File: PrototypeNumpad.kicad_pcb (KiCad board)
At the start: 2 copper layers, 99 x 99 mm, 92 parts, among them J0 Conn_01x06, J1 USB_B_Micro, J1A1 Conn_01x04, Q1 2N7002, SW0 SW_Push, U1 ATmega32U4-AU, U2 USBLC6-2SC6, Y1 Crystal_GND24

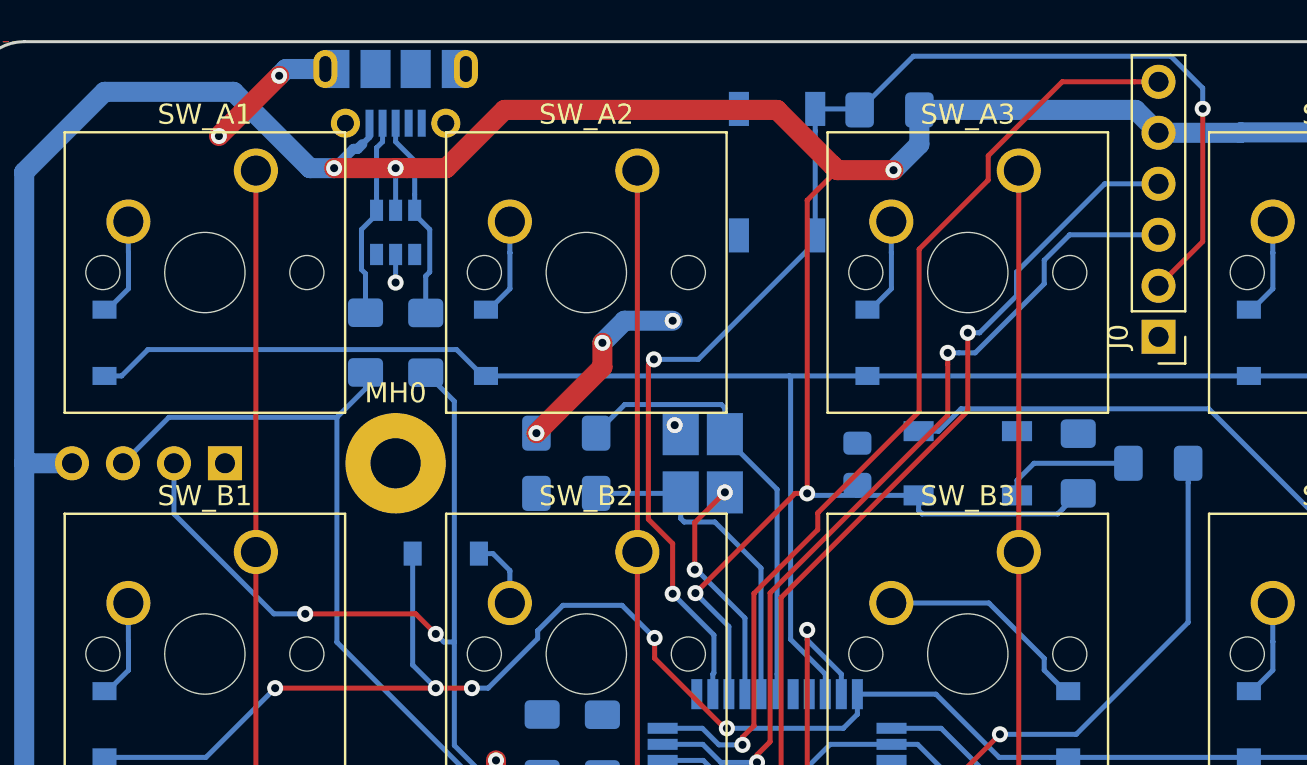
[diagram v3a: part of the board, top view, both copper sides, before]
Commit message: Organize pin headers
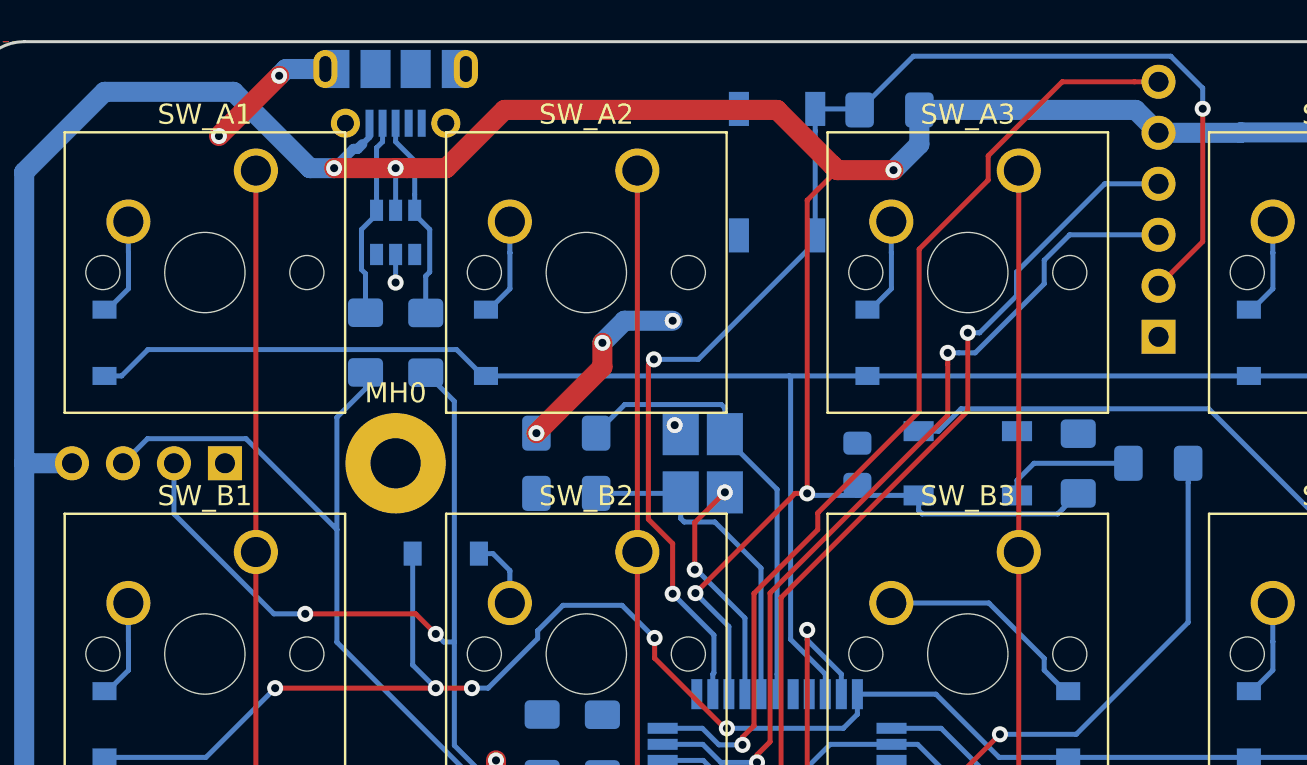
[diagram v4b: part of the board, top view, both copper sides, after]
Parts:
- J0: moved to B.Cu
- turned J0 to 0 degrees
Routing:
- net D-: track 46.3 -> 47.7 mm
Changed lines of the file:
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@@
     (thickness 1.6)
     (drawings 18)
-    (tracks 670)
+    (tracks 672)
     (zones 0)
     (modules 92)
@@
     )
   )
-  (module Connector_PinHeader_2.54mm:PinHeader_1x06_P2.54mm_Vertical (layer F.Cu)
-    (at 107.5 43.2 180)
+  (module Connector_PinHeader_2.54mm:PinHeader_1x06_P2.54mm_Vertical (layer B.Cu)
+    (at 107.5 43.2)
     (descr "Through hole straight pin header, 1x06, 2.54mm pitch, single row")
     (tags "Through hole pin header THT 1x06 2.54mm single row")
-    (fp_text reference J0 (at 2 0 90) (layer F.SilkS)
-      (effects (font (size 1 1) (thickness 0.15)))
+    (fp_text reference J0 (at -2 0 90) (layer B.Fab)
+      (effects (font (size 1 1) (thickness 0.15)) (justify mirror))
     )
-    (fp_text value Conn_01x06 (at 0 15.03 180) (layer F.Fab)
-      (effects (font (size 1 1) (thickness 0.15)))
+    (fp_text value Conn_01x06 (at 0 -15.03) (layer B.Fab)
+      (effects (font (size 1 1) (thickness 0.15)) (justify mirror))
     )
-    (fp_line (start -0.635 -1.27) (end 1.27 -1.27) (layer F.Fab) (width 0.1))
-    (fp_line (start 1.27 -1.27) (end 1.27 13.97) (layer F.Fab) (width 0.1))
-    (fp_line (start 1.27 13.97) (end -1.27 13.97) (layer F.Fab) (width 0.1))
-    (fp_line (start -1.27 13.97) (end -1.27 -0.635) (layer F.Fab) (width 0.1))
-    (fp_line (start -1.27 -0.635) (end -0.635 -1.27) (layer F.Fab) (width 0.1))
-    (fp_line (start -1.33 14.03) (end 1.33 14.03) (layer F.SilkS) (width 0.12))
-    (fp_line (start -1.33 1.27) (end -1.33 14.03) (layer F.SilkS) (width 0.12))
-    (fp_line (start 1.33 1.27) (end 1.33 14.03) (layer F.SilkS) (width 0.12))
-    (fp_line (start -1.33 1.27) (end 1.33 1.27) (layer F.SilkS) (width 0.12))
-    (fp_line (start -1.33 0) (end -1.33 -1.33) (layer F.SilkS) (width 0.12))
-    (fp_line (start -1.33 -1.33) (end 0 -1.33) (layer F.SilkS) (width 0.12))
-    (fp_line (start -1.8 -1.8) (end -1.8 14.5) (layer F.CrtYd) (width 0.05))
-    (fp_line (start -1.8 14.5) (end 1.8 14.5) (layer F.CrtYd) (width 0.05))
-    (fp_line (start 1.8 14.5) (end 1.8 -1.8) (layer F.CrtYd) (width 0.05))
-    (fp_line (start 1.8 -1.8) (end -1.8 -1.8) (layer F.CrtYd) (width 0.05))
-    (fp_text user %R (at 0 6.35 270) (layer F.Fab)
-      (effects (font (size 1 1) (thickness 0.15)))
+    (fp_line (start -0.635 1.27) (end 1.27 1.27) (layer B.Fab) (width 0.1))
+    (fp_line (start 1.27 1.27) (end 1.27 -13.97) (layer B.Fab) (width 0.1))
+    (fp_line (start 1.27 -13.97) (end -1.27 -13.97) (layer B.Fab) (width 0.1))
+    (fp_line (start -1.27 -13.97) (end -1.27 0.635) (layer B.Fab) (width 0.1))
+    (fp_line (start -1.27 0.635) (end -0.635 1.27) (layer B.Fab) (width 0.1))
+    (fp_line (start -1.33 -14.03) (end 1.33 -14.03) (layer B.SilkS) (width 0.12))
+    (fp_line (start -1.33 -1.27) (end -1.33 -14.03) (layer B.SilkS) (width 0.12))
+    (fp_line (start 1.33 -1.27) (end 1.33 -14.03) (layer B.SilkS) (width 0.12))
+    (fp_line (start -1.33 -1.27) (end 1.33 -1.27) (layer B.SilkS) (width 0.12))
+    (fp_line (start -1.33 0) (end -1.33 1.33) (layer B.SilkS) (width 0.12))
+    (fp_line (start -1.33 1.33) (end 0 1.33) (layer B.SilkS) (width 0.12))
+    (fp_line (start -1.8 1.8) (end -1.8 -14.5) (layer B.CrtYd) (width 0.05))
+    (fp_line (start -1.8 -14.5) (end 1.8 -14.5) (layer B.CrtYd) (width 0.05))
+    (fp_line (start 1.8 -14.5) (end 1.8 1.8) (layer B.CrtYd) (width 0.05))
+    (fp_line (start 1.8 1.8) (end -1.8 1.8) (layer B.CrtYd) (width 0.05))
+    (fp_text user %R (at 0 -6.35 -90) (layer B.Fab)
+      (effects (font (size 1 1) (thickness 0.15)) (justify mirror))
     )
-    (pad 1 thru_hole rect (at 0 0 180) (size 1.7 1.7) (drill 1) (layers *.Cu *.Mask)
+    (pad 1 thru_hole rect (at 0 0) (size 1.7 1.7) (drill 1) (layers *.Cu *.Mask)
       (net 1 GND))
-    (pad 2 thru_hole oval (at 0 2.54 180) (size 1.7 1.7) (drill 1) (layers *.Cu *.Mask)
+    (pad 2 thru_hole oval (at 0 -2.54) (size 1.7 1.7) (drill 1) (layers *.Cu *.Mask)
       (net 43 RST))
-    (pad 3 thru_hole oval (at 0 5.08 180) (size 1.7 1.7) (drill 1) (layers *.Cu *.Mask)
+    (pad 3 thru_hole oval (at 0 -5.08) (size 1.7 1.7) (drill 1) (layers *.Cu *.Mask)
       (net 44 MOSI))
-    (pad 4 thru_hole oval (at 0 7.62 180) (size 1.7 1.7) (drill 1) (layers *.Cu *.Mask)
+    (pad 4 thru_hole oval (at 0 -7.62) (size 1.7 1.7) (drill 1) (layers *.Cu *.Mask)
       (net 45 SCK))
-    (pad 5 thru_hole oval (at 0 10.16 180) (size 1.7 1.7) (drill 1) (layers *.Cu *.Mask)
+    (pad 5 thru_hole oval (at 0 -10.16) (size 1.7 1.7) (drill 1) (layers *.Cu *.Mask)
       (net 4 VCC))
-    (pad 6 thru_hole oval (at 0 12.7 180) (size 1.7 1.7) (drill 1) (layers *.Cu *.Mask)
+    (pad 6 thru_hole oval (at 0 -12.7) (size 1.7 1.7) (drill 1) (layers *.Cu *.Mask)
       (net 46 MISO))
     (model ${KISYS3DMOD}/Connector_PinHeader_2.54mm.3dshapes/PinHeader_1x06_P2.54mm_Vertical.wrl
@@
     (descr "Through hole straight pin header, 1x04, 2.54mm pitch, single row")
     (tags "Through hole pin header THT 1x04 2.54mm single row")
-    (fp_text reference J1A1 (at 2 -7.4 -180) (layer B.SilkS)
+    (fp_text reference J1A1 (at 2 -7.4 180) (layer B.Fab)
       (effects (font (size 1 1) (thickness 0.15)) (justify mirror))
     )
@@
   (segment (start 77.263268 69.1) (end 81.8 69.1) (width 0.25) (layer B.Cu) (net 51))
   (segment (start 66.574999 58.411731) (end 77.263268 69.1) (width 0.25) (layer B.Cu) (net 51))
-  (segment (start 66.574999 47.212501) (end 66.574999 58.411731) (width 0.25) (layer B.Cu) (net 51))
   (segment (start 68 45.7875) (end 66.574999 47.212501) (width 0.25) (layer B.Cu) (net 51))
   (segment (start 68 44.975) (end 68 45.7875) (width 0.25) (layer B.Cu) (net 51))
-  (segment (start 58.207499 47.212501) (end 66.574999 47.212501) (width 0.25) (layer B.Cu) (net 51))
-  (segment (start 55.92 49.5) (end 58.207499 47.212501) (width 0.25) (layer B.Cu) (net 51))
+  (segment (start 62.049998 48.274999) (end 66.574999 52.8) (width 0.25) (layer B.Cu) (net 51))
+  (segment (start 57.145001 48.274999) (end 62.049998 48.274999) (width 0.25) (layer B.Cu) (net 51))
+  (segment (start 55.92 49.5) (end 57.145001 48.274999) (width 0.25) (layer B.Cu) (net 51))
+  (segment (start 66.574999 47.212501) (end 66.574999 52.8) (width 0.25) (layer B.Cu) (net 51))
+  (segment (start 66.574999 52.8) (end 66.574999 58.411731) (width 0.25) (layer B.Cu) (net 51))
   (segment (start 94.675 70.7) (end 94.2 70.7) (width 0.25) (layer B.Cu) (net 52))
   (segment (start 97.58391 72.41251) (end 96.38751 72.41251) (width 0.25) (layer B.Cu) (net 52))

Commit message: Add Komi-san to Silkscreen layer
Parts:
- added G***: LOGO, Fate_Parts:Komi, B.Cu at (89.8, 96.2)

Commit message: Update ATmega32u4 decoupling capacitor values
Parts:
- C3: value 0.1uF -> 1uF
- C4: value 1F -> 0.1uF
- C5: value 1uF -> 0.1uF
- C6: value 10uF -> 0.1uF
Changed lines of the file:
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@@
       (effects (font (size 1 1) (thickness 0.15)) (justify mirror))
     )
-    (fp_text value 0.1uF (at 0 -1.82 270) (layer B.Fab)
+    (fp_text value 1uF (at 0 -1.82 270) (layer B.Fab)
       (effects (font (size 1 1) (thickness 0.15)) (justify mirror))
     )
@@
       (effects (font (size 1 1) (thickness 0.15)) (justify mirror))
     )
-    (fp_text value 1F (at 0 -1.82 270) (layer B.Fab)
+    (fp_text value 0.1uF (at 0 -1.82 270) (layer B.Fab)
       (effects (font (size 1 1) (thickness 0.15)) (justify mirror))
     )
@@
       (effects (font (size 1 1) (thickness 0.15)) (justify mirror))
     )
-    (fp_text value 1uF (at 0 -1.82) (layer B.Fab)
+    (fp_text value 0.1uF (at 0 -1.82) (layer B.Fab)
       (effects (font (size 1 1) (thickness 0.15)) (justify mirror))
     )
@@
       (effects (font (size 1 1) (thickness 0.15)) (justify mirror))
     )
-    (fp_text value 10uF (at 0 -1.82 90) (layer B.Fab)
+    (fp_text value 0.1uF (at 0 -1.82 90) (layer B.Fab)
       (effects (font (size 1 1) (thickness 0.15)) (justify mirror))
     )
